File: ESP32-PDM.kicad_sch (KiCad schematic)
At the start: 6 parts, among them J1 5569-08A2-210, J2 Conn_02x06_Top_Bottom

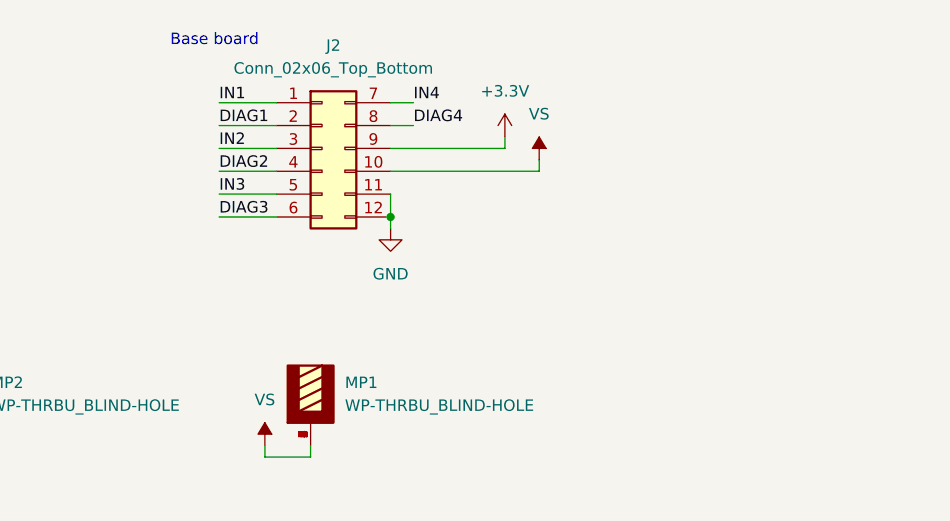
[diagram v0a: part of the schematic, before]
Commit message: Switch to TPS27S100A, replace series diodes with GND network
- U1-U4: TPS27S100APWPR (pin-compatible; TPS1H100A had 11 in stock at
  JLCPCB). Existing footprint is already the TPS27S100 one.
- Remove the PMEG045 series diodes (1.09 USD each, ~2 W loss at 4 A).
  Reverse polarity is handled by the datasheet GND network instead:
  1k || DSK16 from device GND (DGND) to board GND; ILIM resistor and
  thermal pad moved to DGND as the datasheet requires.
- 4.7k series resistors on EN and FLT (datasheet: >= 4.7k on I/O pins).
- 10k FLT pull-up to 3.3 V now lives on the module.
- DIAG_EN pull-up 2.2k -> 4.7k.
- Note: header pin 12 (GND) = MOD_ID 0 for the base board.

ERC unchanged (15 pre-existing power-flag warnings).

Co-Authored-By: Claude Opus 5.5 <noreply@anthropic.com>
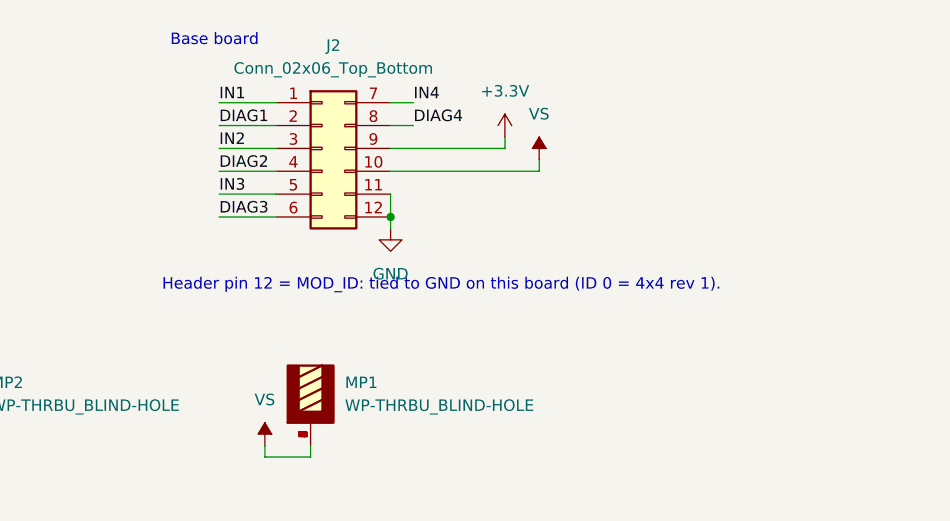
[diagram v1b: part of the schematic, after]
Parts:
- J1: LCSC (none) -> C240833
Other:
- note added: "Header pin 12 = MOD_ID: tied to GND on this board (ID 0 = 4x4 rev 1)."

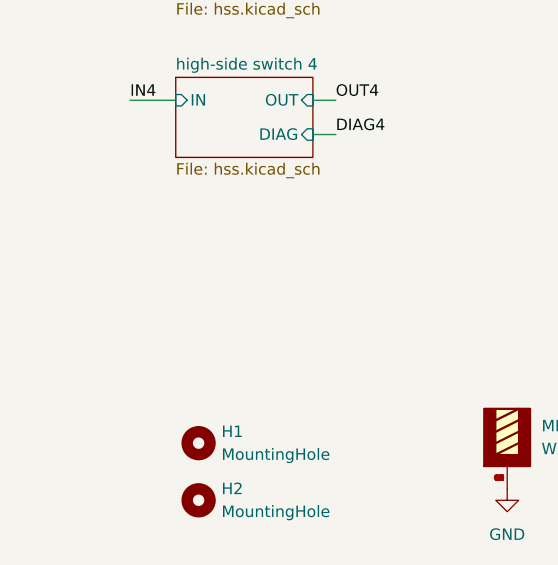
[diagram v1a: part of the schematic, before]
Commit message: Add surge clamp on VS, basic ILIM resistor, clean up ERC
- D5: SMCJ30CA (1.5 kW bidirectional) across VS-GND at the module power
  input. TPS27S100 is 40 V max (48 V < 400 ms); clamp is 48.4 V at 31 A
  and lower at smaller surge currents. Bidirectional so a reversed
  battery is not shorted.
- ILIM resistors 560 R moved to 0603 (basic part C23204).
- ERC: TPS1H100A symbol OUT pins 6/7 passive (paralleled outputs);
  PWR_FLAGs on VS, GND, +3.3V and per-channel DGND.

ERC: 0 violations.

Co-Authored-By: Claude Opus 5.5 <noreply@anthropic.com>
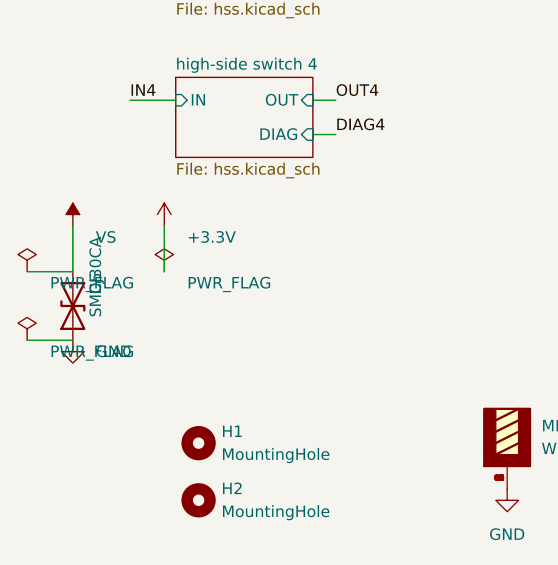
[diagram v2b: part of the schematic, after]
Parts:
- added D5: SMCJ30CA, Diode_SMD:D_SMC, symbol Device:D_TVS
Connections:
- net GND: now also D5.1 (A1)
- net VS: now also D5.2 (A2)
